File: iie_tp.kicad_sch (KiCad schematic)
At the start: 47 parts, among them J1 Conn_01x03, J2 Conn_01x02, J3 Conn_01x01, J4 Conn_01x01, J5 Conn_01x02, J6 Conn_01x02, J7 Conn_01x03, J8 AudioJack2_Ground, U1 ${SIM.PARAMS}, U2 LM386

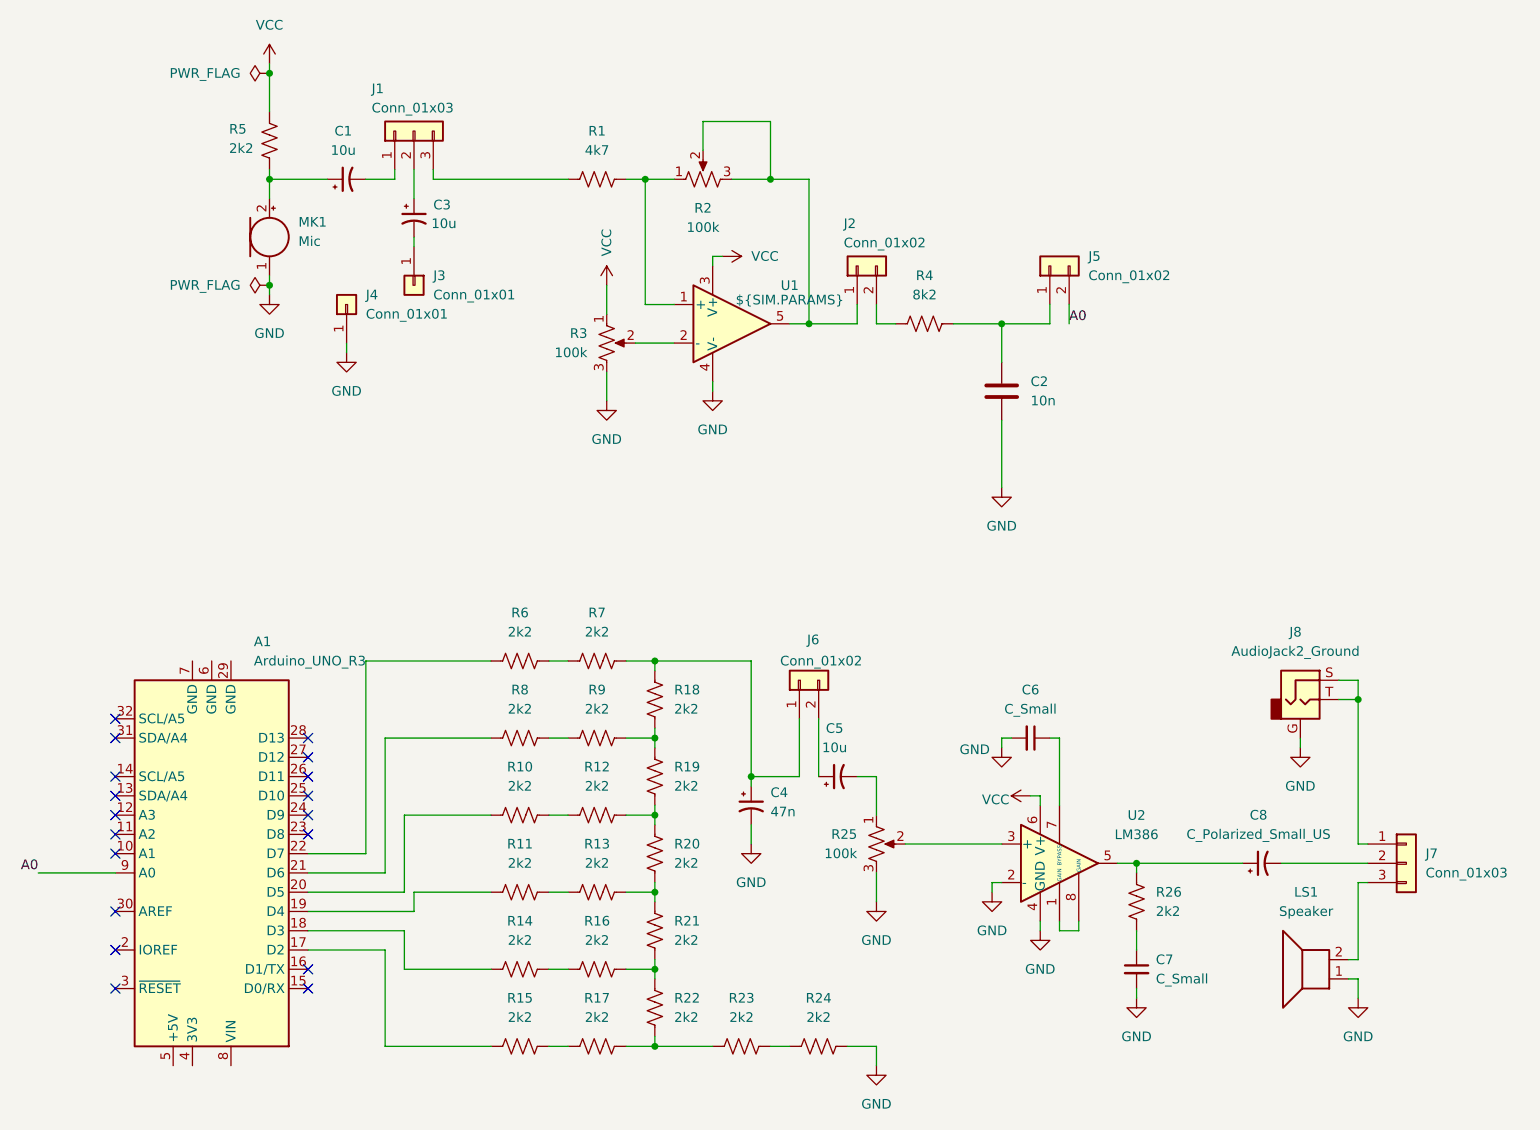
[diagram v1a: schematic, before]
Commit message: fix: Errores DRC del esquemático
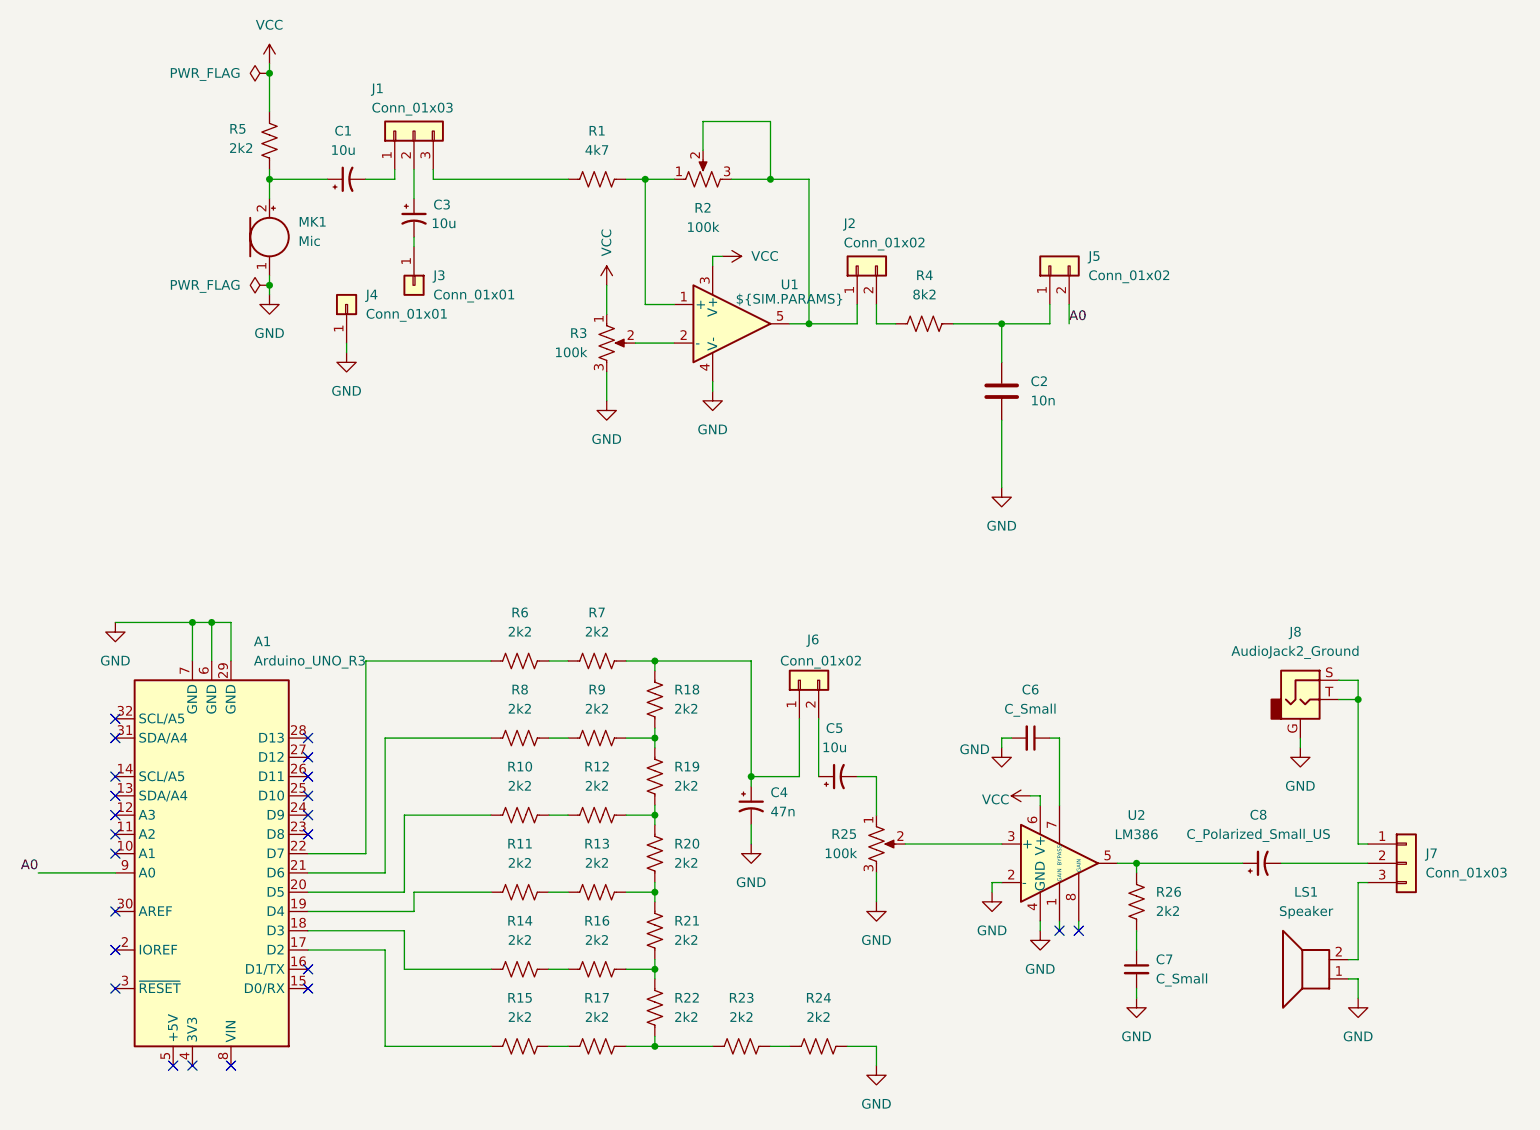
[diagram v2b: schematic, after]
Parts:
- U1: footprint Package_DIP:DIP-14_W7.62mm -> (none)
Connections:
- net GND: now also A1.29 (GND), A1.6 (GND), A1.7 (GND)
- net at U2.1 (GAIN): no longer U2.8 (GAIN)
- no-connect marks 18 -> 23
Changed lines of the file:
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@@
 	)
 	(junction
+		(at 44.45 101.6)
+		(diameter 0)
+		(color 0 0 0 0)
+	)
+	(junction
 		(at 125.73 62.23)
 		(diameter 0)
@@
 	)
 	(junction
+		(at 46.99 101.6)
+		(diameter 0)
+		(color 0 0 0 0)
+	)
+	(junction
 		(at 105.41 116.84)
 		(diameter 0)
@@
 	)
 	(no_connect
+		(at 161.29 142.24)
+	)
+	(no_connect
 		(at 59.69 129.54)
 	)
 	(no_connect
+		(at 44.45 160.02)
+	)
+	(no_connect
 		(at 59.69 149.86)
 	)
@@
 	)
 	(no_connect
+		(at 158.75 142.24)
+	)
+	(no_connect
 		(at 34.29 129.54)
 	)
 	(no_connect
+		(at 49.53 160.02)
+	)
+	(no_connect
 		(at 59.69 147.32)
 	)
@@
 	)
 	(no_connect
+		(at 41.91 160.02)
+	)
+	(no_connect
 		(at 59.69 121.92)
 	)
@@
 	(wire
 		(pts
-			(xy 158.75 142.24) (xy 161.29 142.24)
-		)
-		(stroke
-			(width 0)
-			(type default)
-		)
-	)
-	(wire
-		(pts
 			(xy 118.11 123.19) (xy 118.11 121.92)
 		)
@@
 	(wire
 		(pts
+			(xy 34.29 101.6) (xy 44.45 101.6)
+		)
+		(stroke
+			(width 0)
+			(type default)
+		)
+	)
+	(wire
+		(pts
 			(xy 67.31 106.68) (xy 67.31 132.08)
 		)
@@
 	(wire
 		(pts
+			(xy 46.99 106.68) (xy 46.99 101.6)
+		)
+		(stroke
+			(width 0)
+			(type default)
+		)
+	)
+	(wire
+		(pts
 			(xy 123.19 62.23) (xy 125.73 62.23)
 		)
@@
 	(wire
 		(pts
+			(xy 49.53 101.6) (xy 49.53 106.68)
+		)
+		(stroke
+			(width 0)
+			(type default)
+		)
+	)
+	(wire
+		(pts
 			(xy 195.58 111.76) (xy 198.12 111.76)
 		)
@@
 	(wire
 		(pts
+			(xy 44.45 101.6) (xy 46.99 101.6)
+		)
+		(stroke
+			(width 0)
+			(type default)
+		)
+	)
+	(wire
+		(pts
 			(xy 54.61 57.15) (xy 54.61 58.42)
 		)
@@
 	(wire
 		(pts
+			(xy 44.45 106.68) (xy 44.45 101.6)
+		)
+		(stroke
+			(width 0)
+			(type default)
+		)
+	)
+	(wire
+		(pts
 			(xy 127 114.3) (xy 127 121.92)
 		)
@@
 	(wire
 		(pts
+			(xy 46.99 101.6) (xy 49.53 101.6)
+		)
+		(stroke
+			(width 0)
+			(type default)
+		)
+	)
+	(wire
+		(pts
 			(xy 76.2 41.91) (xy 76.2 43.18)
 		)
@@
 	)
 	(symbol
+		(lib_id "power:GND")
+		(at 34.29 101.6 0)
+		(unit 1)
+		(exclude_from_sim no)
+		(in_bom yes)
+		(on_board yes)
+		(dnp no)
+		(fields_autoplaced yes)
+		(property "Reference" "#PWR019"
+			(at 34.29 107.95 0)
+			(effects
+				(font
+					(size 1.27 1.27)
+				)
+				(hide yes)
+			)
+		)
+		(property "Value" "GND"
+			(at 34.29 106.68 0)
+			(effects
+				(font
+					(size 1.27 1.27)
+				)
+			)
+		)
+		(property "Footprint" ""
+			(at 34.29 101.6 0)
+			(effects
+				(font
+					(size 1.27 1.27)
+				)
+				(hide yes)
+			)
+		)
+		(property "Datasheet" ""
+			(at 34.29 101.6 0)
+			(effects
+				(font
+					(size 1.27 1.27)
+				)
+				(hide yes)
+			)
+		)
+		(property "Description" "Power symbol creates a global label with name \"GND\" , ground"
+			(at 34.29 101.6 0)
+			(effects
+				(font
+					(size 1.27 1.27)
+				)
+				(hide yes)
+			)
+		)
+		(pin "1"
+		)
+		(instances
+			(project ""
+				(path "/f91fc3da-5f4a-447d-a72e-43c2dd640f87"
+					(reference "#PWR019")
+					(unit 1)
+				)
+			)
+		)
+	)
+	(symbol
+		(lib_name "OPAMP_1")
+		(lib_id "Simulation_SPICE:OPAMP")
+		(at 115.57 62.23 0)
+		(unit 1)
+		(exclude_from_sim no)
+		(in_bom yes)
+		(on_board yes)
+		(dnp no)
+		(fields_autoplaced yes)
+		(property "Reference" "U1"
+			(at 123.19 57.0798 0)
+			(effects
+				(font
+					(size 1.27 1.27)
+				)
+			)
+		)
+		(property "Value" "${SIM.PARAMS}"
+			(at 123.19 58.9849 0)
+			(effects
+				(font
+					(size 1.27 1.27)
+				)
+			)
+		)
+		(property "Footprint" ""
+			(at 115.57 62.23 0)
+			(effects
+				(font
+					(size 1.27 1.27)
+				)
+				(hide yes)
+			)
+		)
+		(property "Datasheet" "https://ngspice.sourceforge.io/docs/ngspice-html-manual/manual.xhtml#sec__SUBCKT_Subcircuits"
+			(at 115.57 62.23 0)
+			(effects
+				(font
+					(size 1.27 1.27)
+				)
+				(hide yes)
+			)
+		)
+		(property "Description" "Operational amplifier, single"
+			(at 115.57 62.23 0)
+			(effects
+				(font
+					(size 1.27 1.27)
+				)
+				(hide yes)
+			)
+		)
+		(property "Sim.Pins" "1=in+ 2=in- 3=vcc 4=vee 5=out"
+			(at 115.57 62.23 0)
+			(effects
+				(font
+					(size 1.27 1.27)
+				)
+				(hide yes)
+			)
+		)
+		(property "Sim.Device" "SUBCKT"
+			(at 115.57 62.23 0)
+			(effects
+				(font
+					(size 1.27 1.27)
+				)
+				(justify left)
+				(hide yes)
+			)
+		)
+		(property "Sim.Library" "${KICAD9_SYMBOL_DIR}/Simulation_SPICE.sp"
+			(at 115.57 62.23 0)
+			(effects
+				(font
+					(size 1.27 1.27)
+				)
+				(hide yes)
+			)
+		)
+		(property "Sim.Name" "kicad_builtin_opamp"
+			(at 115.57 62.23 0)
+			(effects
+				(font
+					(size 1.27 1.27)
+				)
+				(hide yes)
+			)
+		)
+		(pin "5"
+		)
+		(pin "4"
+		)
+		(pin "1"
+		)
+		(pin "2"
+		)
+		(pin "3"
+		)
+		(instances
+			(project ""
+				(path "/f91fc3da-5f4a-447d-a72e-43c2dd640f87"
+					(reference "U1")
+					(unit 1)
+				)
+			)
+		)
+	)
+	(symbol
 		(lib_id "Device:C_Polarized_Small_US")
 		(at 129.54 121.92 90)
@@
 					(unit 1)
 				)
-			)
-		)
-	)
-	(symbol
-		(lib_id "Simulation_SPICE:OPAMP")
-		(at 115.57 62.23 0)
-		(unit 1)
-		(exclude_from_sim no)
-		(in_bom yes)
-		(on_board yes)
-		(dnp no)
-		(fields_autoplaced yes)
-		(property "Reference" "U1"
-			(at 123.19 57.1814 0)
-			(effects
-				(font
-					(size 1.27 1.27)
-				)
-			)
-		)
-		(property "Value" "${SIM.PARAMS}"
-			(at 123.19 59.0865 0)
-			(effects
-				(font
-					(size 1.27 1.27)
-				)
-			)
-		)
-		(property "Footprint" "Package_DIP:DIP-14_W7.62mm"
-			(at 115.57 62.23 0)
-			(effects
-				(font
-					(size 1.27 1.27)
-				)
-				(hide yes)
-			)
-		)
-		(property "Datasheet" "https://ngspice.sourceforge.io/docs/ngspice-html-manual/manual.xhtml#sec__SUBCKT_Subcircuits"
-			(at 115.57 62.23 0)
-			(effects
-				(font
-					(size 1.27 1.27)
-				)
-				(hide yes)
-			)
-		)
-		(property "Description" "Operational amplifier, single, node sequence=1:+ 2:- 3:OUT 4:V+ 5:V-"
-			(at 115.57 62.23 0)
-			(effects
-				(font
-					(size 1.27 1.27)
-				)
-				(hide yes)
-			)
-		)
-		(property "Sim.Pins" "1=in+ 2=in- 3=vcc 4=vee 5=out"
-			(at 115.57 62.23 0)
-			(effects
-				(font
-					(size 1.27 1.27)
-				)
-				(hide yes)
-			)
-		)
-		(property "Sim.Device" "SUBCKT"
-			(at 115.57 62.23 0)
-			(effects
-				(font
-					(size 1.27 1.27)
-				)
-				(justify left)
-				(hide yes)
-			)
-		)
-		(property "Sim.Library" "${KICAD7_SYMBOL_DIR}/Simulation_SPICE.sp"
-			(at 115.57 62.23 0)
-			(effects
-				(font
-					(size 1.27 1.27)
-				)
-				(hide yes)
-			)
-		)
-		(property "Sim.Name" "kicad_builtin_opamp"
-			(at 115.57 62.23 0)
-			(effects
-				(font
-					(size 1.27 1.27)
-				)
-				(hide yes)
-			)
-		)
-		(pin "4"
-		)
-		(pin "3"
-		)
-		(pin "5"
-		)
-		(pin "1"
-		)
-		(pin "2"
-		)
-		(instances
-			(project ""
-				(path "/f91fc3da-5f4a-447d-a72e-43c2dd640f87"
-					(reference "U1")
-					(unit 1)
-				)
